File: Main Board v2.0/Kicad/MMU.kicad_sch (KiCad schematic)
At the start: 6 parts, among them U2 GLT725608, U3 74HCT574, U4 74HCT574, U5 GLT725608, U6 74HC245, U7 74HC245

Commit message: update
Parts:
- added C10, C11, C12, C13, C8, C9: 100n, symbol Device:C
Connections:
- net +5V: now also C10.1, C11.1, C12.1, C13.1, C8.1, C9.1
- net GND: now also C10.2, C11.2, C12.2, C13.2, C8.2, C9.2
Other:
- note added: "TBD: Remove the latches and let the CPLD control the SRAM A0-A14 directly."

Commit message: schematic done*
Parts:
- removed U3, U4: 74HCT574, symbol 74xx:74HCT574
- C1: renamed from C8; footprint (none) -> Capacitor_SMD:C_0603_1608Metric_Pad1.08x0.95mm_HandSolder
- C2: renamed from C9; footprint (none) -> Capacitor_SMD:C_0603_1608Metric_Pad1.08x0.95mm_HandSolder
- C3: renamed from C10; footprint (none) -> Capacitor_SMD:C_0603_1608Metric_Pad1.08x0.95mm_HandSolder
- C4: renamed from C11; footprint (none) -> Capacitor_SMD:C_0603_1608Metric_Pad1.08x0.95mm_HandSolder
- C5: renamed from C12; footprint (none) -> Capacitor_SMD:C_0603_1608Metric_Pad1.08x0.95mm_HandSolder
- C6: renamed from C13; footprint (none) -> Capacitor_SMD:C_0603_1608Metric_Pad1.08x0.95mm_HandSolder
- U3: renamed from U6; footprint (none) -> Package_SO:TSSOP-20-1EP_4.4x6.5mm_P0.65mm_EP2.15x3.35mm
- U4: renamed from U7; footprint (none) -> Package_SO:TSSOP-20-1EP_4.4x6.5mm_P0.65mm_EP2.15x3.35mm
- renumbered U2 to U1, U5 to U2
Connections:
- net MMU_MAP7: now reaches U1.21 (A10), U2.21 (A10)
- net MMU_MAP6: now reaches U1.24 (A9), U2.24 (A9)
- net MMU_MAP5: now reaches U1.25 (A8), U2.25 (A8)
- net MMU_MAP4: now reaches U1.3 (A7), U2.3 (A7)
- net MMU_MAP3: now reaches U1.4 (A6), U2.4 (A6)
- net MMU_MAP2: now reaches U1.5 (A5), U2.5 (A5)
- net MMU_MAP1: now reaches U1.6 (A4), U2.6 (A4)
- net MMU_MAP0: now reaches U1.7 (A3), U2.7 (A3)
- net MA26 renamed MMU_MP_RD
- net MA27 renamed MMU_MP_WR
- net MA28 renamed MMU_MP_EXE
- net MMU_MAP_SEL0 renamed MMU_MAP8
- net MMU_MAP_SEL1 renamed MMU_MAP9
- net MMU_MAP_SEL2 renamed MMU_MAP10
- net MMU_MAP_SEL3 renamed MMU_MAP11
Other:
- note removed: "MMU_IOL_XX signals manage the latch that holds the memory map address for programming the MMU memory pages."
- note removed: "MMU_MAP_SELn allows selecting 16 memory maps that can be isolated from each other (multi-tasking)."
- note removed: "MMU_MEML_XX signals manage the latch that holds the memory map address for executing code."
- note removed: "One latch for executing code. One latch for programming the lookup table SRAMs"
- note removed: "Some (3) of these MA lines could also be used to implement memory protection. Read, Write and Execute."
- note removed: "TBD: Remove the latches and let the CPLD control the SRAM A0-A14 directly."
- moved on the sheet: C1, C2, C3, C4, C5, C6, U1, U2, U3, U4

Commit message: board update
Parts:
- removed U1, U2: GLT725608, Package_SO:SOJ-28_7.62x18.415mm_P1.27mm, symbol Memory_RAM:IS62C256AL
- added U10, U11: CY7C109B, Package_SO:SOJ-32_10.16x20.955mm_P1.27mm, symbol Memory_RAM:IS6xC1024AL-xxK
- U3, U4: value 74HC245 -> 74HCT245; footprint Package_SO:TSSOP-20-1EP_4.4x6.5mm_P0.65mm_EP2.15x3.35mm -> Package_DIP:CERDIP-20_W7.62mm_SideBrazed_LongPads_Socket
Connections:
- net +5V: now also U10.30 (CS2/CE2), U10.32 (VCC), U11.30 (CS2/CE2), U11.32 (VCC)
- net A13: now also U10.12 (A0), U11.12 (A0)
- net A14: now also U10.11 (A1), U11.11 (A1)
- net A15: now also U10.10 (A2), U11.10 (A2)
- net GND: now also U10.16 (GND), U11.16 (GND)
- net MA13: now also U10.13 (I/O0)
- net MA14: now also U10.14 (I/O1)
- net MA15: now also U10.15 (I/O2)
- net MA16: now also U10.17 (I/O3)
- net MA17: now also U10.18 (I/O4)
- net MA18: now also U10.19 (I/O5)
- net MA19: now also U10.20 (I/O6)
- net MA20: now also U10.21 (I/O7)
- net MA21: now also U11.13 (I/O0)
- net MA22: now also U11.14 (I/O1)
- net MA23: now also U11.15 (I/O2)
- net MA24: now also U11.17 (I/O3)
- net MA25: now also U11.18 (I/O4)
- net MMU_MAP0: now also U10.9 (A3), U11.9 (A3)
- net MMU_MAP1: now also U10.8 (A4), U11.8 (A4)
- net MMU_MAP10: now also U10.28 (A13), U11.28 (A13)
- net MMU_MAP11: now also U10.3 (A14), U11.3 (A14)
- net MMU_MAP2: now also U10.7 (A5), U11.7 (A5)
- net MMU_MAP3: now also U10.6 (A6), U11.6 (A6)
- net MMU_MAP4: now also U10.5 (A7), U11.5 (A7)
- net MMU_MAP5: now also U10.27 (A8), U11.27 (A8)
- net MMU_MAP6: now also U10.26 (A9), U11.26 (A9)
- net MMU_MAP7: now also U10.23 (A10), U11.23 (A10)
- net MMU_MAP8: now also U10.25 (A11), U11.25 (A11)
- net MMU_MAP9: now also U10.4 (A12), U11.4 (A12)
- net MMU_MP_EXE: now also U11.21 (I/O7)
- net MMU_MP_RD: now also U11.19 (I/O5)
- net MMU_MP_WR: now also U11.20 (I/O6)
- net ~{MMU_RAM1_CE}: now also U10.22 (~{CS1}/~{CE1})
- net ~{MMU_RAM1_OE}: now also U10.24 (~{OE})
- net ~{MMU_RAM1_WE}: now also U10.29 (~{WE})
- net ~{MMU_RAM2_CE}: now also U11.22 (~{CS1}/~{CE1})
- net ~{MMU_RAM2_OE}: now also U11.24 (~{OE})
- net ~{MMU_RAM2_WE}: now also U11.29 (~{WE})
- new net MMU_MAP12: U10.31 (A15), U11.31 (A15)
- new net MMU_MAP13: U10.2 (A16), U11.2 (A16)
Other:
- note removed: "Fast Cache SRAM (12-15ns)"
- moved on the sheet: U3

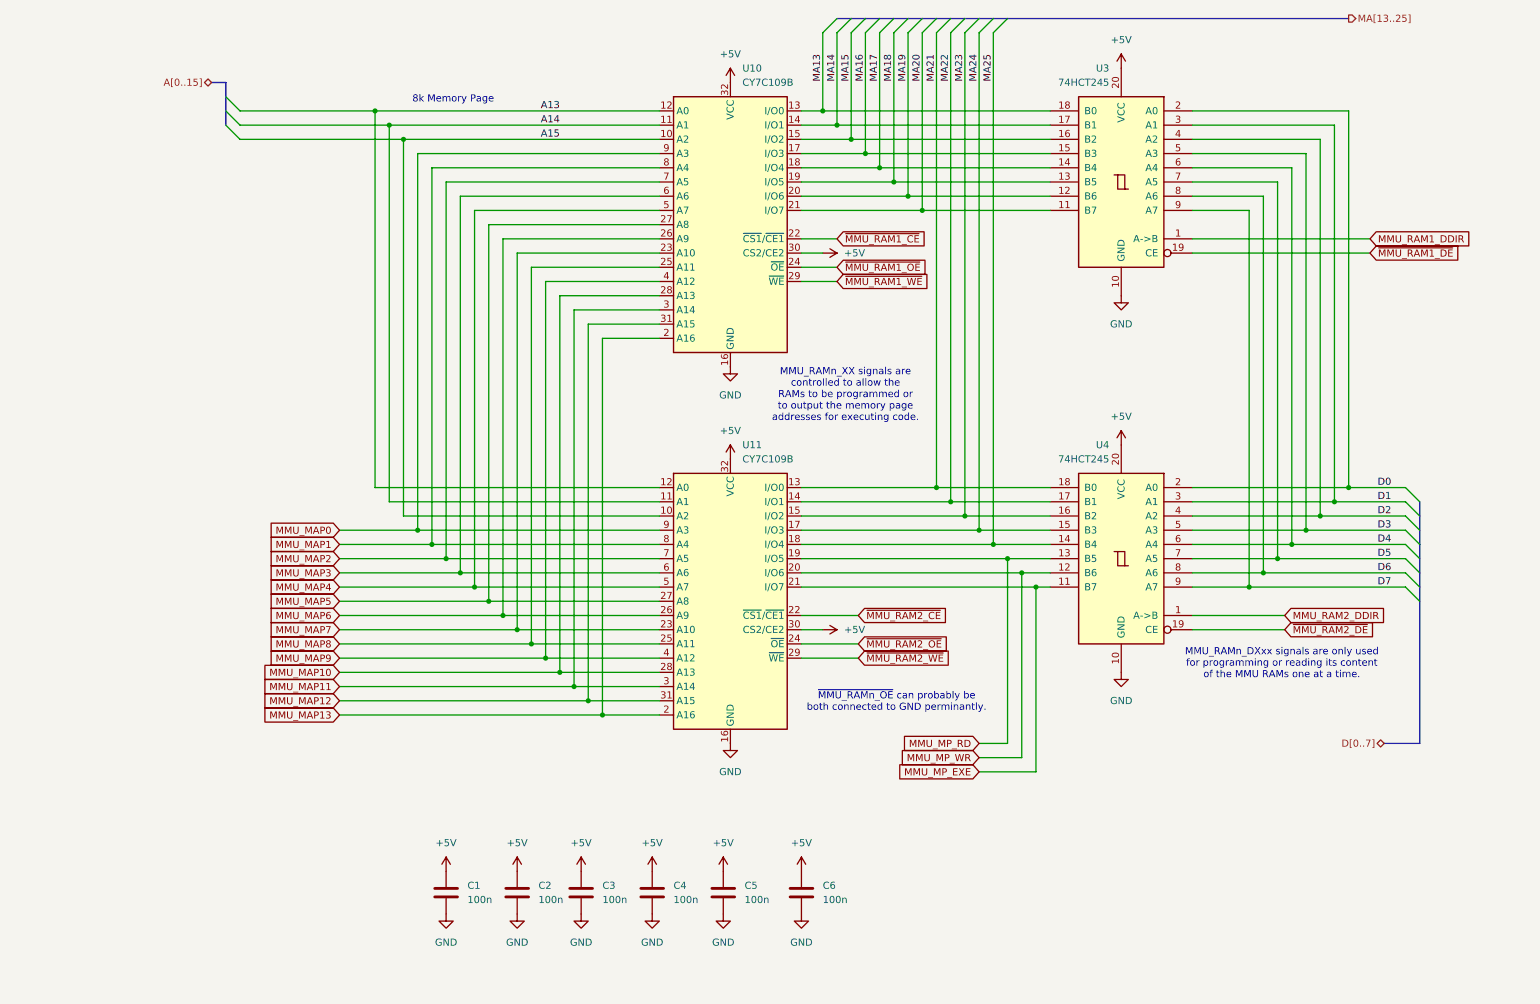
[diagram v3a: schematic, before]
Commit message: schematic update
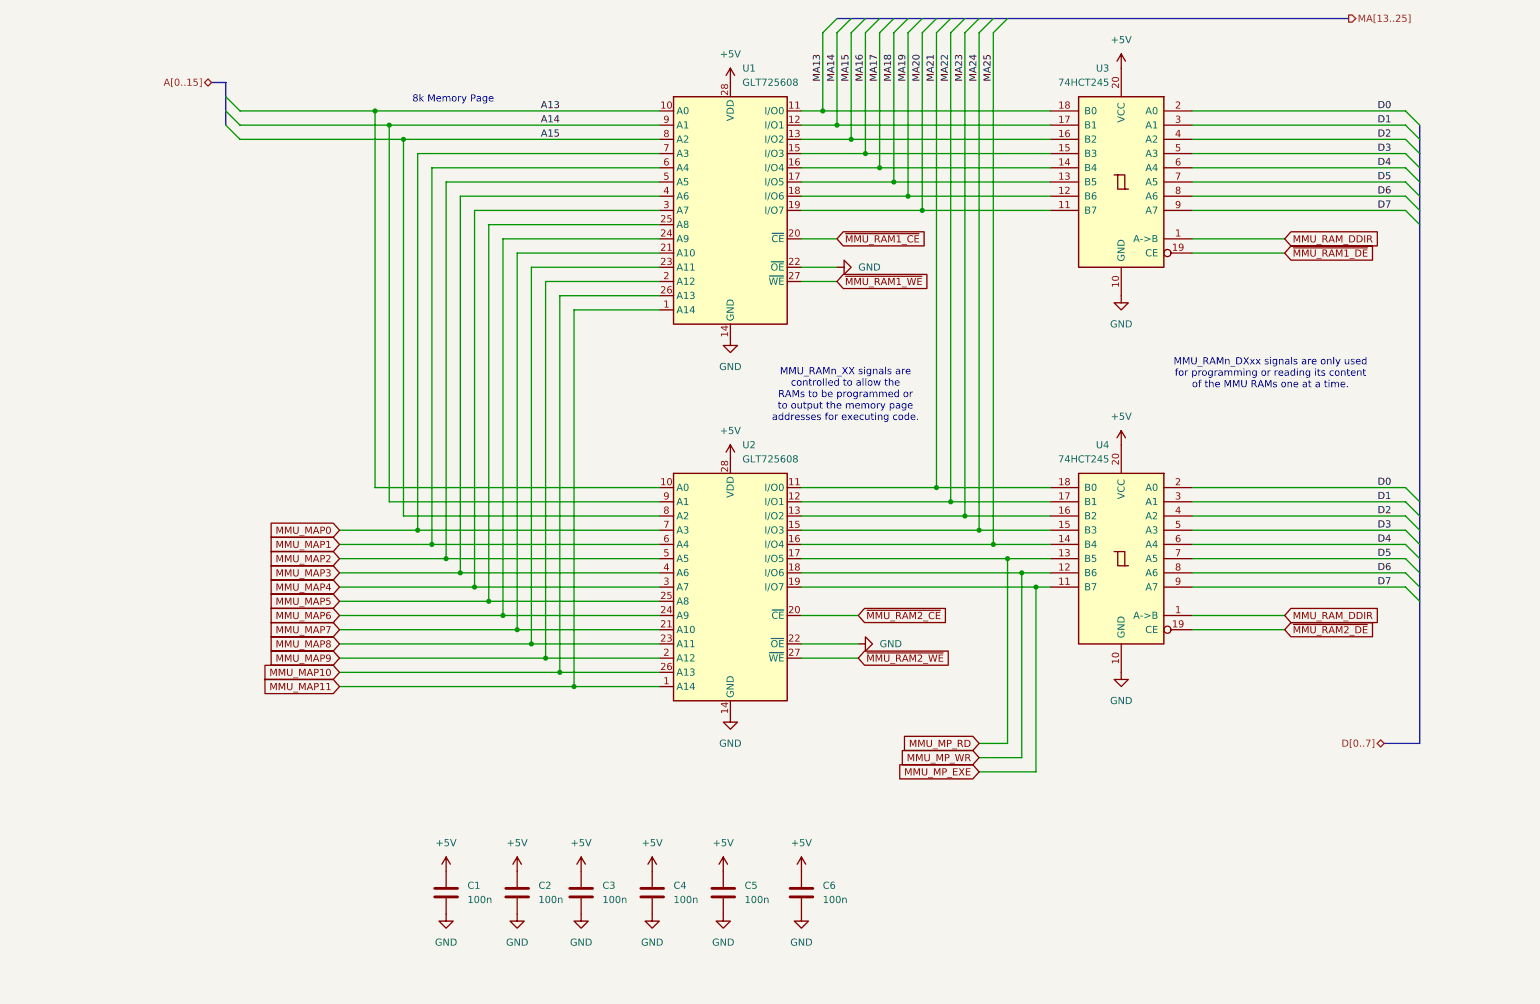
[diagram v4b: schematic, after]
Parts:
- removed U10, U11: CY7C109B, Package_SO:SOJ-32_10.16x20.955mm_P1.27mm, symbol Memory_RAM:IS6xC1024AL-xxK
- added U1, U2: GLT725608, Package_SO:SOJ-28_7.62x18.415mm_P1.27mm, symbol Memory_RAM:IS65C256AL
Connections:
- net MMU_RAM2_DDIR is gone; now on net MMU_RAM_DDIR: U4.1 (A->B)
- net +5V: now also U1.28 (VDD), U2.28 (VDD)
- net A13: now also U1.10 (A0), U2.10 (A0)
- net A14: now also U1.9 (A1), U2.9 (A1)
- net A15: now also U1.8 (A2), U2.8 (A2)
- net GND: now also U1.14 (GND), U1.22 (~{OE}), U2.14 (GND), U2.22 (~{OE})
- net MA13: now also U1.11 (I/O0)
- net MA14: now also U1.12 (I/O1)
- net MA15: now also U1.13 (I/O2)
- net MA16: now also U1.15 (I/O3)
- net MA17: now also U1.16 (I/O4)
- net MA18: now also U1.17 (I/O5)
- net MA19: now also U1.18 (I/O6)
- net MA20: now also U1.19 (I/O7)
- net MA21: now also U2.11 (I/O0)
- net MA22: now also U2.12 (I/O1)
- net MA23: now also U2.13 (I/O2)
- net MA24: now also U2.15 (I/O3)
- net MA25: now also U2.16 (I/O4)
- net MMU_MAP0: now also U1.7 (A3), U2.7 (A3)
- net MMU_MAP1: now also U1.6 (A4), U2.6 (A4)
- net MMU_MAP10: now also U1.26 (A13), U2.26 (A13)
- net MMU_MAP11: now also U1.1 (A14), U2.1 (A14)
- net MMU_MAP2: now also U1.5 (A5), U2.5 (A5)
- net MMU_MAP3: now also U1.4 (A6), U2.4 (A6)
- net MMU_MAP4: now also U1.3 (A7), U2.3 (A7)
- net MMU_MAP5: now also U1.25 (A8), U2.25 (A8)
- net MMU_MAP6: now also U1.24 (A9), U2.24 (A9)
- net MMU_MAP7: now also U1.21 (A10), U2.21 (A10)
- net MMU_MAP8: now also U1.23 (A11), U2.23 (A11)
- net MMU_MAP9: now also U1.2 (A12), U2.2 (A12)
- net MMU_MP_EXE: now also U2.19 (I/O7)
- net MMU_MP_RD: now also U2.17 (I/O5)
- net MMU_MP_WR: now also U2.18 (I/O6)
- net ~{MMU_RAM1_CE}: now also U1.20 (~{CE})
- net ~{MMU_RAM1_WE}: now also U1.27 (~{WE})
- net ~{MMU_RAM2_CE}: now also U2.20 (~{CE})
- net ~{MMU_RAM2_WE}: now also U2.27 (~{WE})
- net MMU_RAM1_DDIR renamed MMU_RAM_DDIR
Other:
- note removed: "~{MMU_RAMn_OE} can probably be both connected to GND perminantly."

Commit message: schematic updates
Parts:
- removed C5, C6: 100n, Capacitor_SMD:C_0603_1608Metric_Pad1.08x0.95mm_HandSolder, symbol Device:C
- added R1, R10, R11, R12, R13, R14, R15, R16, R17, R18, R19, R2, R20, R21, R22, R23, R24, R25, R26, R3, R4, R5, R6, R7, R8, R9: 10k, Resistor_SMD:R_0603_1608Metric_Pad0.98x0.95mm_HandSolder, symbol Device:R_Small
- renumbered U3 to U1, U1 to U2, U4 to U3, U2 to U4
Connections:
- net +5V: now also R1.1, R10.1, R11.1, R12.1, R13.1, R2.1, R3.1, R4.1, R5.1, R6.1, R7.1, R8.1, R9.1
- net D0: now also U1.18 (B0), U3.18 (B0); no longer U1.2 (A0), U3.2 (A0)
- net D1: now also U1.17 (B1), U3.17 (B1); no longer U1.3 (A1), U3.3 (A1)
- net D2: now also U1.16 (B2), U3.16 (B2); no longer U1.4 (A2), U3.4 (A2)
- net D3: now also U1.15 (B3), U3.15 (B3); no longer U1.5 (A3), U3.5 (A3)
- net D4: now also U1.14 (B4), U3.14 (B4); no longer U1.6 (A4), U3.6 (A4)
- net D5: now also U1.13 (B5), U3.13 (B5); no longer U1.7 (A5), U3.7 (A5)
- net D6: now also U1.12 (B6), U3.12 (B6); no longer U1.8 (A6), U3.8 (A6)
- net D7: now also U1.11 (B7), U3.11 (B7); no longer U1.9 (A7), U3.9 (A7)
- net GND: now also R14.2, R15.2, R16.2, R17.2, R18.2, R19.2, R20.2, R21.2, R22.2, R23.2, R24.2, R25.2, R26.2
- net MA13: now also U1.2 (A0), R14.1, R7.2; no longer U1.18 (B0)
- net MA14: now also U1.3 (A1), R1.2, R21.1; no longer U1.17 (B1)
- net MA15: now also U1.4 (A2), R15.1, R8.2; no longer U1.16 (B2)
- net MA16: now also U1.5 (A3), R2.2, R22.1; no longer U1.15 (B3)
- net MA17: now also U1.6 (A4), R16.1, R9.2; no longer U1.14 (B4)
- net MA18: now also U1.7 (A5), R23.1, R3.2; no longer U1.13 (B5)
- net MA19: now also U1.8 (A6), R10.2, R17.1; no longer U1.12 (B6)
- net MA20: now also U1.9 (A7), R24.1, R4.2; no longer U1.11 (B7)
- net MA21: now also U3.2 (A0), R11.2, R18.1; no longer U3.18 (B0)
- net MA22: now also U3.3 (A1), R25.1, R5.2; no longer U3.17 (B1)
- net MA23: now also U3.4 (A2), R12.2, R19.1; no longer U3.16 (B2)
- net MA24: now also U3.5 (A3), R26.1, R6.2; no longer U3.15 (B3)
- net MA25: now also U3.6 (A4), R13.2, R20.1; no longer U3.14 (B4)
- net MMU_MP_EXE: now also U3.9 (A7); no longer U3.11 (B7)
- net MMU_MP_RD: now also U3.7 (A5); no longer U3.13 (B5)
- net MMU_MP_WR: now also U3.8 (A6); no longer U3.12 (B6)
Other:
- note added: "RD/~{WR}"
- note added: "Startup Memory Page Only place (13) Rs for desired page address."
- moved on the sheet: C1, C2, C3, C4, U1, U2, U3, U4

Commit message: board
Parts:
- U1, U3: footprint Package_DIP:CERDIP-20_W7.62mm_SideBrazed_LongPads_Socket -> Package_DIP:DIP-20_W7.62mm_Socket_LongPads
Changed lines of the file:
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@@
 			)
 		)
-		(property "Footprint" "Package_DIP:CERDIP-20_W7.62mm_SideBrazed_LongPads_Socket"
+		(property "Footprint" "Package_DIP:DIP-20_W7.62mm_Socket_LongPads"
 			(at 194.31 123.19 0)
 			(hide yes)
@@
 			)
 		)
-		(property "Footprint" "Package_DIP:CERDIP-20_W7.62mm_SideBrazed_LongPads_Socket"
+		(property "Footprint" "Package_DIP:DIP-20_W7.62mm_Socket_LongPads"
 			(at 194.31 55.88 0)
 			(hide yes)

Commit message: board update
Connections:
- net MA25 is gone; now on net MA24: R13.2, R20.1, U3.6 (A4), U4.16 (I/O4)
- net MMU_MAP11 is gone; now on net MMU_MAP10: U2.1 (A14), U4.1 (A14)
- net A13: now also U2.9 (A1), U4.9 (A1); no longer U2.10 (A0), U4.10 (A0)
- net A14: now also U2.8 (A2), U4.8 (A2); no longer U2.9 (A1), U4.9 (A1)
- net A15: now also U2.7 (A3), U4.7 (A3); no longer U2.8 (A2), U4.8 (A2)
- net MA13: now also R1.2, R21.1, U1.3 (A1), U2.12 (I/O1); no longer R14.1, R7.2, U1.2 (A0), U2.11 (I/O0)
- net MA14: now also R15.1, R8.2, U1.4 (A2), U2.13 (I/O2); no longer R1.2, R21.1, U1.3 (A1), U2.12 (I/O1)
- net MA15: now also R2.2, R22.1, U1.5 (A3), U2.15 (I/O3); no longer R15.1, R8.2, U1.4 (A2), U2.13 (I/O2)
- net MA16: now also R16.1, R9.2, U1.6 (A4), U2.16 (I/O4); no longer R2.2, R22.1, U1.5 (A3), U2.15 (I/O3)
- net MA17: now also R23.1, R3.2, U1.7 (A5), U2.17 (I/O5); no longer R16.1, R9.2, U1.6 (A4), U2.16 (I/O4)
- net MA18: now also R10.2, R17.1, U1.8 (A6), U2.18 (I/O6); no longer R23.1, R3.2, U1.7 (A5), U2.17 (I/O5)
- net MA19: now also R24.1, R4.2, U1.9 (A7), U2.19 (I/O7); no longer R10.2, R17.1, U1.8 (A6), U2.18 (I/O6)
- net MA20: now also R11.2, R18.1, U3.2 (A0), U4.11 (I/O0); no longer R24.1, R4.2, U1.9 (A7), U2.19 (I/O7)
- net MA21: now also R25.1, R5.2, U3.3 (A1), U4.12 (I/O1); no longer R11.2, R18.1, U3.2 (A0), U4.11 (I/O0)
- net MA22: now also R12.2, R19.1, U3.4 (A2), U4.13 (I/O2); no longer R25.1, R5.2, U3.3 (A1), U4.12 (I/O1)
- net MA23: now also R26.1, R6.2, U3.5 (A3), U4.15 (I/O3); no longer R12.2, R19.1, U3.4 (A2), U4.13 (I/O2)
- net MA24: no longer R26.1, R6.2, U3.5 (A3), U4.15 (I/O3)
- net MMU_MAP0: now also U2.6 (A4), U4.6 (A4); no longer U2.7 (A3), U4.7 (A3)
- net MMU_MAP1: now also U2.5 (A5), U4.5 (A5); no longer U2.6 (A4), U4.6 (A4)
- net MMU_MAP10: no longer U2.26 (A13), U4.26 (A13)
- net MMU_MAP2: now also U2.4 (A6), U4.4 (A6); no longer U2.5 (A5), U4.5 (A5)
- net MMU_MAP3: now also U2.3 (A7), U4.3 (A7); no longer U2.4 (A6), U4.4 (A6)
- net MMU_MAP4: now also U2.25 (A8), U4.25 (A8); no longer U2.3 (A7), U4.3 (A7)
- net MMU_MAP5: now also U2.24 (A9), U4.24 (A9); no longer U2.25 (A8), U4.25 (A8)
- net MMU_MAP6: now also U2.21 (A10), U4.21 (A10); no longer U2.24 (A9), U4.24 (A9)
- net MMU_MAP7: now also U2.23 (A11), U4.23 (A11); no longer U2.21 (A10), U4.21 (A10)
- net MMU_MAP8: now also U2.2 (A12), U4.2 (A12); no longer U2.23 (A11), U4.23 (A11)
- net MMU_MAP9: now also U2.26 (A13), U4.26 (A13); no longer U2.2 (A12), U4.2 (A12)
- new net A12: U2.10 (A0), U4.10 (A0)
- new net MA12: R14.1, R7.2, U1.2 (A0), U2.11 (I/O0)
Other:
- note added: "4k Memory Page"
- note removed: "8k Memory Page"

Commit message: board update
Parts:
- C1, C2, C3, C4, R1, R10, R11, R12, R13, R14, R15, R16, R17, R18, R19, R2, R20, R21, R22, R23, R24, R25, R26, R3, R4, R5, R6, R7, R8, R9: KiLib_Generator (none) -> SMD_2terminal_chip_molded
- U1, U3: KiLib_Generator (none) -> package/DIP/legacy
- U2, U4: KiLib_Generator (none) -> package/gullwing
